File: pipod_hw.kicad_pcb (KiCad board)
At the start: 2 copper layers, 55.5 x 98.2 mm, 4 parts, among them J1 SFV8R-2STE1HLF, J2 SFV14R-2STE1HLF, J3 Conn_01x03_Male, J7 USB_C_Receptacle_USB2.0

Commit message: drc: set DRC for JLCPCB
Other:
- copper layers 2 -> 4
- board text added: "Layers: 4 PCB thickness: 0.8mm Impedance: Yes (JLC7628)"
- board text removed: "Board thickness: 0.8mm"
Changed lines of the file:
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@@
 (kicad_pcb (version 20211014) (generator pcbnew)
   (general
-    (thickness 1.6)
+    (thickness 0.7412)
   )
   (paper "A4")
   (layers
     (0 "F.Cu" signal)
+    (1 "In1.Cu" signal)
+    (2 "In2.Cu" signal)
     (31 "B.Cu" signal)
     (32 "B.Adhes" user "B.Adhesive")
@@
   )
   (setup
+    (stackup
+      (layer "F.SilkS" (type "Top Silk Screen") (color "White"))
+      (layer "F.Paste" (type "Top Solder Paste"))
+      (layer "F.Mask" (type "Top Solder Mask") (color "Purple") (thickness 0.01))
+      (layer "F.Cu" (type "copper") (thickness 0.035))
+      (layer "dielectric 1" (type "prepreg") (thickness 0.2104) (material "FR4") (epsilon_r 4.5) (loss_tangent 0.02))
+      (layer "In1.Cu" (type "copper") (thickness 0.0152))
+      (layer "dielectric 2" (type "core") (thickness 0.2) (material "FR4") (epsilon_r 4.5) (loss_tangent 0.02))
+      (layer "In2.Cu" (type "copper") (thickness 0.0152))
+      (layer "dielectric 3" (type "prepreg") (thickness 0.2104) (material "FR4") (epsilon_r 4.5) (loss_tangent 0.02))
+      (layer "B.Cu" (type "copper") (thickness 0.035))
+      (layer "B.Mask" (type "Bottom Solder Mask") (color "Purple") (thickness 0.01))
+      (layer "B.Paste" (type "Bottom Solder Paste"))
+      (layer "B.SilkS" (type "Bottom Silk Screen") (color "White"))
+      (copper_finish "None")
+      (dielectric_constraints yes)
+    )
     (pad_to_mask_clearance 0)
     (pcbplotparams
@@
     (effects (font (size 1 1) (thickness 0.15)) (justify left))
   )
-  (gr_text "Board thickness: 0.8mm" (at 133.9 29.2) (layer "Cmts.User")
-    (effects (font (size 5 5) (thickness 0.5)))
+  (gr_text "Layers: 4\nPCB thickness: 0.8mm\nImpedance: Yes (JLC7628)\n" (at 164.81 54.63) (layer "Cmts.User")
+    (effects (font (size 5 5) (thickness 0.5)) (justify left))
   )
   (segment (start 124.248 61.712) (end 124.256999 61.720999) (width 0.25) (layer "F.Cu") (net 0))

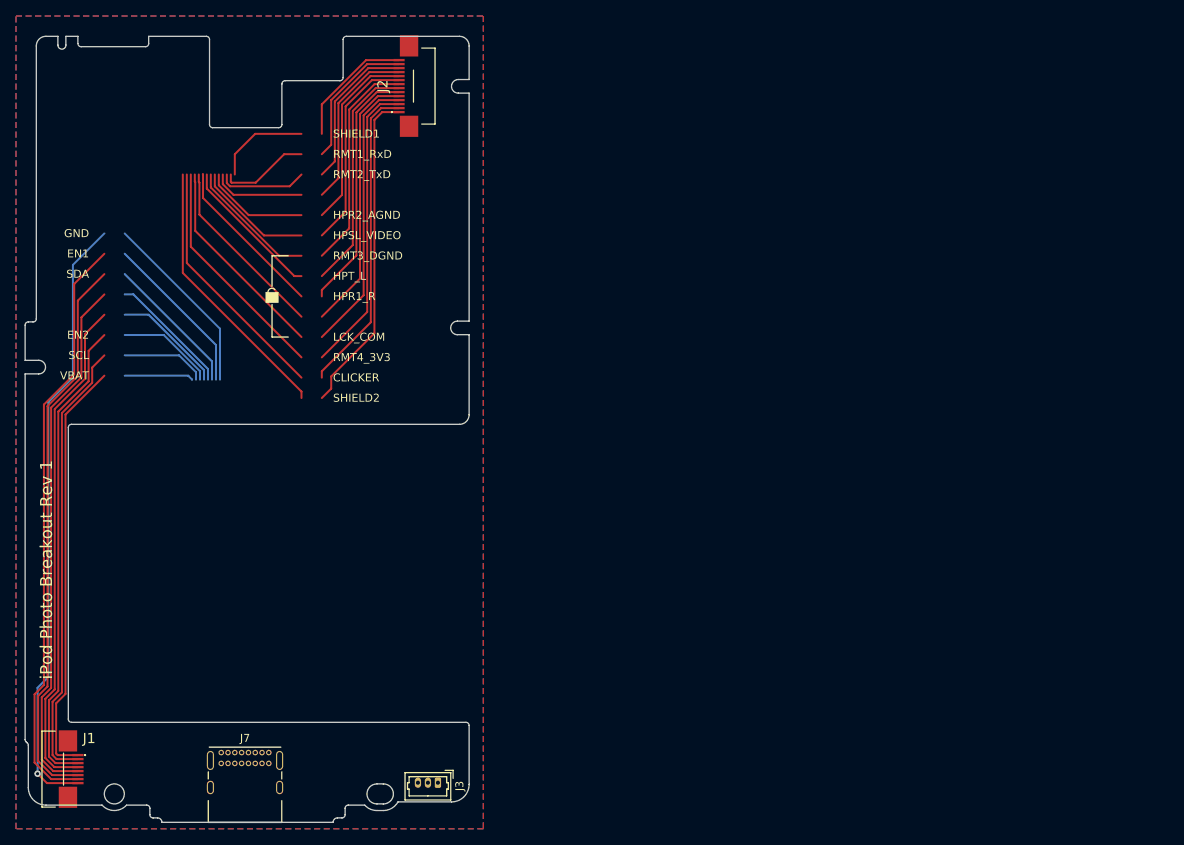
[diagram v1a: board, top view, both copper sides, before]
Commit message: analysis: specify pi will be powered directly from VCC
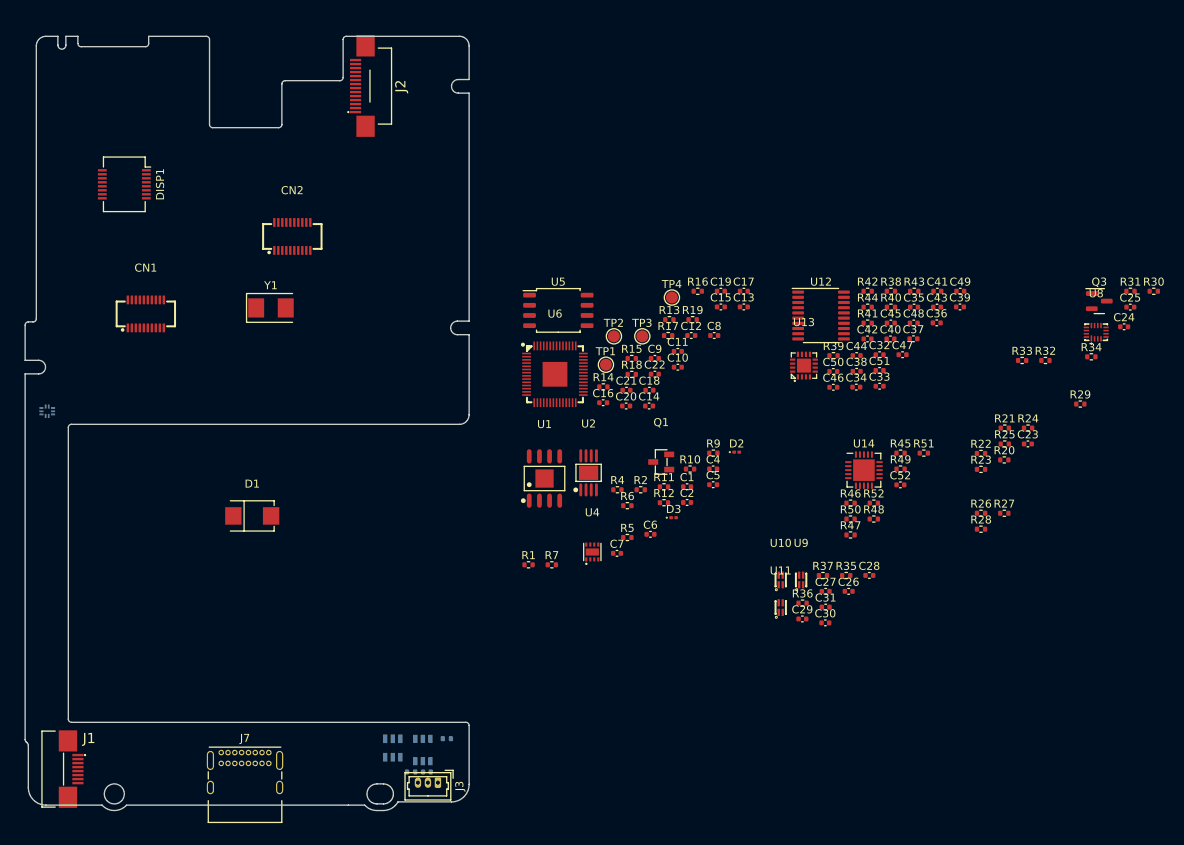
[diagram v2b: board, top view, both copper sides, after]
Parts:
- added C1: 100n, Capacitor_SMD:C_0402_1005Metric, F.Cu at (184.8, 100.7)
- added C10: 100n, Capacitor_SMD:C_0402_1005Metric, F.Cu at (183.6, 85.8)
- added C11: 100n, Capacitor_SMD:C_0402_1005Metric, F.Cu at (183.6, 83.8)
- added C12: 100n, Capacitor_SMD:C_0402_1005Metric, F.Cu at (185.3, 81.8)
- added C13: 100n, Capacitor_SMD:C_0402_1005Metric, F.Cu at (191.9, 78.3)
- added C14: 1u, Capacitor_SMD:C_0402_1005Metric, F.Cu at (180.0, 90.7)
- added C15: 100n, Capacitor_SMD:C_0402_1005Metric, F.Cu at (189.0, 78.3)
- added C16: 100n, Capacitor_SMD:C_0402_1005Metric, F.Cu at (174.3, 90.2)
- added C17: 100n, Capacitor_SMD:C_0402_1005Metric, F.Cu at (191.9, 76.3)
- added C18: 100n, Capacitor_SMD:C_0402_1005Metric, F.Cu at (180.1, 88.7)
- added C19: 100n, Capacitor_SMD:C_0402_1005Metric, F.Cu at (189.0, 76.3)
- added C2: 100n, Capacitor_SMD:C_0402_1005Metric, F.Cu at (184.8, 102.7)
- added C20: 1u, Capacitor_SMD:C_0402_1005Metric, F.Cu at (177.2, 90.7)
- added C21: 30p, Capacitor_SMD:C_0402_1005Metric, F.Cu at (177.2, 88.7)
- added C22: 30p, Capacitor_SMD:C_0402_1005Metric, F.Cu at (180.7, 86.7)
- added C23: 100n, Capacitor_SMD:C_0402_1005Metric, F.Cu at (227.4, 95.4)
- added C24: 100n, Capacitor_SMD:C_0402_1005Metric, F.Cu at (239.4, 80.8)
- added C25: 10u, Capacitor_SMD:C_0402_1005Metric, F.Cu at (240.2, 78.3)
- added C26: 10u, Capacitor_SMD:C_0402_1005Metric, F.Cu at (205.0, 113.8)
- added C27: 10u, Capacitor_SMD:C_0402_1005Metric, F.Cu at (202.1, 113.8)
- added C28: 10u, Capacitor_SMD:C_0402_1005Metric, F.Cu at (207.6, 111.8)
- added C29: 10u, Capacitor_SMD:C_0402_1005Metric, F.Cu at (199.2, 117.3)
- added C3: 100n, Capacitor_SMD:C_0402_1005Metric, B.Cu at (152.2, 136.4)
- added C30: 10u, Capacitor_SMD:C_0402_1005Metric, F.Cu at (202.1, 117.8)
- added C31: 10u, Capacitor_SMD:C_0402_1005Metric, F.Cu at (202.1, 115.8)
- added C32: 10u, Capacitor_SMD:C_0402_1005Metric, F.Cu at (208.8, 84.2)
- added C33: 100n, Capacitor_SMD:C_0402_1005Metric, F.Cu at (208.8, 88.2)
- added C34: 10u, Capacitor_SMD:C_0402_1005Metric, F.Cu at (205.9, 88.3)
- added C35: 100n, Capacitor_SMD:C_0402_1005Metric, F.Cu at (213.1, 78.3)
- added C36: 10u, Capacitor_SMD:C_0402_1005Metric, F.Cu at (216.0, 80.3)
- added C37: 100n, Capacitor_SMD:C_0402_1005Metric, F.Cu at (213.1, 82.2)
- added C38: 10u, Capacitor_SMD:C_0402_1005Metric, F.Cu at (206.0, 86.3)
- added C39: 2.2u, Capacitor_SMD:C_0402_1005Metric, F.Cu at (218.9, 78.3)
- added C4: 10u, Capacitor_SMD:C_0402_1005Metric, F.Cu at (188.0, 98.5)
- added C40: 2.2u, Capacitor_SMD:C_0402_1005Metric, F.Cu at (210.2, 82.3)
- added C41: 100n, Capacitor_SMD:C_0402_1005Metric, F.Cu at (216.1, 76.3)
- added C42: 10u, Capacitor_SMD:C_0402_1005Metric, F.Cu at (207.3, 82.3)
- added C43: 100n, Capacitor_SMD:C_0402_1005Metric, F.Cu at (216.0, 78.3)
- added C44: 1u, Capacitor_SMD:C_0402_1005Metric, F.Cu at (206.0, 84.3)
- added C45: 1u, Capacitor_SMD:C_0402_1005Metric, F.Cu at (210.2, 80.3)
- added C46: 2.2u, Capacitor_SMD:C_0402_1005Metric, F.Cu at (203.1, 88.3)
- added C47: 1u, Capacitor_SMD:C_0402_1005Metric, F.Cu at (211.7, 84.2)
- added C48: 1u, Capacitor_SMD:C_0402_1005Metric, F.Cu at (213.1, 80.3)
- added C49: 1u, Capacitor_SMD:C_0402_1005Metric, F.Cu at (218.9, 76.3)
- added C5: 100n, Capacitor_SMD:C_0402_1005Metric, F.Cu at (188.0, 100.5)
- added C50: 1u, Capacitor_SMD:C_0402_1005Metric, F.Cu at (203.1, 86.3)
- added C51: 1u, Capacitor_SMD:C_0402_1005Metric, F.Cu at (208.8, 86.2)
- added C52: 100n, Capacitor_SMD:C_0402_1005Metric, F.Cu at (211.4, 100.5)
- added C6: 100n, Capacitor_SMD:C_0402_1005Metric, F.Cu at (180.2, 106.7)
- added C7: 10u, Capacitor_SMD:C_0402_1005Metric, F.Cu at (176.0, 109.1)
- added C8: 100n, Capacitor_SMD:C_0402_1005Metric, F.Cu at (188.2, 81.8)
- added C9: 100n, Capacitor_SMD:C_0402_1005Metric, F.Cu at (180.7, 84.7)
- added CN1: 539160208, lcsc:CONN-SMD_539160208, F.Cu at (117.1, 79.1)
- added CN2: 539160208, lcsc:CONN-SMD_539160208, F.Cu at (135.4, 69.5)
- added D1: MBRS130LT3G, lcsc:SMB_L4.6-W3.6-LS5.3-RD, F.Cu at (130.4, 104.4)
- added D2: RED, LED_SMD:LED_0201_0603Metric, F.Cu at (191.0, 96.4)
- added D3: GRN, LED_SMD:LED_0201_0603Metric, F.Cu at (183.1, 104.6)
- added DISP1: STP240320_0200B, Connector_Molex:Molex_SlimStack_54722-0164_2x08_P0.50mm_Vertical, F.Cu at (114.4, 62.9)
- added Q1: DMP1045U-7, lcsc:SOT-23-3_L2.9-W1.3-P1.90-LS2.4-BR, F.Cu at (181.5, 97.7)
- added Q2: UMW8205A, lcsc:SOT-23-6_L2.9-W1.6-P0.95-LS2.8-BL, B.Cu at (148.0, 133.4)
- added Q3: BSS138, Package_TO_SOT_SMD:SOT-23, F.Cu at (236.3, 77.5)
- added R1: 10k, Resistor_SMD:R_0402_1005Metric, F.Cu at (164.9, 110.5)
- added R10: 10k, Resistor_SMD:R_0402_1005Metric, F.Cu at (185.1, 98.5)
- added R11: 5.36k, Resistor_SMD:R_0402_1005Metric, F.Cu at (181.9, 100.8)
- added R12: 1.62k, Resistor_SMD:R_0402_1005Metric, F.Cu at (181.9, 102.7)
- added R13: 10k, Resistor_SMD:R_0402_1005Metric, F.Cu at (182.6, 79.9)
- added R14: DNP, Resistor_SMD:R_0402_1005Metric, F.Cu at (174.3, 88.3)
- added R15: 1k, Resistor_SMD:R_0402_1005Metric, F.Cu at (177.8, 84.7)
- added R16: 10k, Resistor_SMD:R_0402_1005Metric, F.Cu at (186.1, 76.3)
- added R17: 27R, Resistor_SMD:R_0402_1005Metric, F.Cu at (182.4, 81.8)
- added R18: 27R, Resistor_SMD:R_0402_1005Metric, F.Cu at (177.8, 86.7)
- added R19: 10k, Resistor_SMD:R_0402_1005Metric, F.Cu at (185.5, 79.9)
- added R2: 1.62k 2%, Resistor_SMD:R_0402_1005Metric, F.Cu at (179.0, 101.1)
- added R20: DNP, Resistor_SMD:R_0402_1005Metric, F.Cu at (224.4, 97.4)
- added R21: 10k, Resistor_SMD:R_0402_1005Metric, F.Cu at (224.5, 93.4)
- added R22: 15k, Resistor_SMD:R_0402_1005Metric, F.Cu at (221.5, 96.6)
- added R23: 5.1k, Resistor_SMD:R_0402_1005Metric, F.Cu at (221.5, 98.6)
- added R24: 5.1k, Resistor_SMD:R_0402_1005Metric, F.Cu at (227.4, 93.4)
- added R25: 10k, Resistor_SMD:R_0402_1005Metric, F.Cu at (224.5, 95.4)
- added R26: 10k, Resistor_SMD:R_0402_1005Metric, F.Cu at (221.5, 104.1)
- added R27: 100k, Resistor_SMD:R_0402_1005Metric, F.Cu at (224.4, 104.1)
- added R28: 10k, Resistor_SMD:R_0402_1005Metric, F.Cu at (221.5, 106.0)
- added R29: 10k, Resistor_SMD:R_0402_1005Metric, F.Cu at (233.9, 90.4)
- added R3: 1k, Resistor_SMD:R_0402_1005Metric, B.Cu at (154.7, 132.2)
- added R30: 0R, Resistor_SMD:R_0402_1005Metric, F.Cu at (243.1, 76.3)
- added R31: 10k, Resistor_SMD:R_0402_1005Metric, F.Cu at (240.2, 76.3)
- added R32: 10k, Resistor_SMD:R_0402_1005Metric, F.Cu at (229.6, 85.0)
- added R33: 10R, Resistor_SMD:R_0402_1005Metric, F.Cu at (226.7, 85.0)
- added R34: 0R, Resistor_SMD:R_0402_1005Metric, F.Cu at (235.3, 84.5)
- added R35: 10k, Resistor_SMD:R_0402_1005Metric, F.Cu at (204.7, 111.8)
- added R36: 10k, Resistor_SMD:R_0402_1005Metric, F.Cu at (199.2, 115.3)
- added R37: 10k, Resistor_SMD:R_0402_1005Metric, F.Cu at (201.8, 111.8)
- added R38: 10k, Resistor_SMD:R_0402_1005Metric, F.Cu at (210.2, 76.3)
- added R39: 10k, Resistor_SMD:R_0402_1005Metric, F.Cu at (203.1, 84.4)
- added R4: 5.62k 2%, Resistor_SMD:R_0402_1005Metric, F.Cu at (176.1, 101.1)
- added R40: 10k, Resistor_SMD:R_0402_1005Metric, F.Cu at (210.2, 78.3)
- added R41: 10k, Resistor_SMD:R_0402_1005Metric, F.Cu at (207.3, 80.3)
- added R42: 10k, Resistor_SMD:R_0402_1005Metric, F.Cu at (207.3, 76.3)
- added R43: 10k, Resistor_SMD:R_0402_1005Metric, F.Cu at (213.2, 76.3)
- added R44: 10k, Resistor_SMD:R_0402_1005Metric, F.Cu at (207.3, 78.3)
- added R45: 10k, Resistor_SMD:R_0402_1005Metric, F.Cu at (211.4, 96.5)
- added R46: 0R, Resistor_SMD:R_0402_1005Metric, F.Cu at (205.2, 102.8)
- added R47: 0R, Resistor_SMD:R_0402_1005Metric, F.Cu at (205.2, 106.8)
- added R48: 0R, Resistor_SMD:R_0402_1005Metric, F.Cu at (208.1, 104.8)
- added R49: 0R, Resistor_SMD:R_0402_1005Metric, F.Cu at (211.4, 98.5)
- added R5: 1.27M 2%, Resistor_SMD:R_0402_1005Metric, F.Cu at (177.3, 107.1)
- added R50: 0R, Resistor_SMD:R_0402_1005Metric, F.Cu at (205.2, 104.8)
- added R51: 0R, Resistor_SMD:R_0402_1005Metric, F.Cu at (214.4, 96.5)
- added R52: 0R, Resistor_SMD:R_0402_1005Metric, F.Cu at (208.1, 102.8)
- added R6: 1k, Resistor_SMD:R_0402_1005Metric, F.Cu at (177.3, 103.1)
- added R7: 1k, Resistor_SMD:R_0402_1005Metric, F.Cu at (167.9, 110.5)
- added R8: 470R, Resistor_SMD:R_0402_1005Metric, B.Cu at (150.3, 136.4)
- added R9: 10k, Resistor_SMD:R_0402_1005Metric, F.Cu at (188.1, 96.5)
- added TP1: TestPoint, TestPoint:TestPoint_Pad_D1.5mm, F.Cu at (174.6, 85.5)
- added TP2: TestPoint, TestPoint:TestPoint_Pad_D1.5mm, F.Cu at (175.6, 81.9)
- added TP3: TestPoint, TestPoint:TestPoint_Pad_D1.5mm, F.Cu at (179.2, 81.9)
- added TP4: TestPoint, TestPoint:TestPoint_Pad_D1.5mm, F.Cu at (182.9, 77.1)
- added U1: TD5830B, lcsc:SOP-8_L4.9-W3.9-P1.27-LS6.0-BL-EP, F.Cu at (166.9, 99.7)
- added U10: SY6283ADRC, lcsc:DFN-4_L1.6-W1.2-P0.50-BL, F.Cu at (196.5, 112.4)
- added U11: SY6283ADRC, lcsc:DFN-4_L1.6-W1.2-P0.50-BL, F.Cu at (196.5, 115.8)
- added U12: PCM5102, Package_SO:TSSOP-20_4.4x6.5mm_P0.65mm, F.Cu at (201.5, 79.3)
- added U13: PAM8908JER, lcsc:QFN-16_L3.0-W3.0-P0.50-BL-EP1.7, F.Cu at (199.4, 85.6)
- added U14: MCP23008-xML, Package_DFN_QFN:QFN-20-1EP_4x4mm_P0.5mm_EP2.7x2.7mm, F.Cu at (206.9, 98.7)
- added U2: TP4056M, lcsc:MSOP-8_L3.0-W3.0-P0.65-LS5.0-BL-EP, F.Cu at (172.5, 99.0)
- added U3: DW01A-G, lcsc:SOT-23-6_L2.9-W1.6-P0.95-LS2.8-BR, B.Cu at (151.7, 133.7)
- added U4: MAX17048G+T10, lcsc:DFN-8_L2.0-W2.0-P0.50-BL-EP, F.Cu at (172.9, 108.9)
- added U5: W25Q128JVS, Package_SO:SOIC-8_5.23x5.23mm_P1.27mm, F.Cu at (168.7, 78.7)
- added U6: RP2040, lcsc:LQFN-56_L7.0-W7.0-P0.4-EP, F.Cu at (168.2, 86.7)
- added U7: PI3USB102EZLEX, lcsc:TQFN-10_L1.6-W1.3-P0.50-BL, B.Cu at (104.8, 91.3)
- added U8: TS3A5018RSVR, lcsc:UQFN-16_L2.6-W1.8-P0.40-BL, F.Cu at (235.9, 81.4)
- added U9: SY6283ADRC, lcsc:DFN-4_L1.6-W1.2-P0.50-BL, F.Cu at (199.0, 112.4)
- added Y1: 12MHz 20pF, Crystal:Crystal_SMD_5032-2Pin_5.0x3.2mm, F.Cu at (132.8, 78.4)
- moved J2 5.44 mm to (145.1, 50.7)
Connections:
- net Net-(J7-PadA4) renamed VBUS
- J1 pad 1: unconnected-(J1-Pad1) -> +3V3
- J1 pad 2: unconnected-(J1-Pad2) -> SMC_CW_SCK
- J1 pad 3: unconnected-(J1-Pad3) -> CW_EN1
- J1 pad 6: unconnected-(J1-Pad6) -> SMC_CW_MOSI
- J1 pad 7: unconnected-(J1-Pad7) -> CW_EN2
- J1 pad 8: unconnected-(J1-Pad8) -> GND
- J2 pad 1: unconnected-(J2-Pad1) -> HP_SHIELD
- J2 pad 10: unconnected-(J2-Pad10) -> GNDA
- J2 pad 12: unconnected-(J2-Pad12) -> SMC_RMT_TX
- J2 pad 13: unconnected-(J2-Pad13) -> SMC_RMT_RX
- J2 pad 14: unconnected-(J2-Pad14) -> HP_SHIELD
- J2 pad 2: unconnected-(J2-Pad2) -> HP_CLICKER
- J2 pad 3: unconnected-(J2-Pad3) -> HP_RMT4_3V3
- J2 pad 4: unconnected-(J2-Pad4) -> HP_LCK
- J2 pad 6: unconnected-(J2-Pad6) -> HP_R1_R
- J2 pad 7: unconnected-(J2-Pad7) -> HP_T_L
- J2 pad 8: unconnected-(J2-Pad8) -> GND
- J2 pad 9: unconnected-(J2-Pad9) -> HP_SL_VIDEO
- J7 pad A1: Net-(J7-PadA1) -> GND
- J7 pad A12: Net-(J7-PadA1) -> GND
- J7 pad A5: unconnected-(J7-PadA5) -> USB_CC1
- J7 pad A6: unconnected-(J7-PadA6) -> USB_D+
- J7 pad A7: unconnected-(J7-PadA7) -> USB_D-
- J7 pad B1: Net-(J7-PadA1) -> GND
- J7 pad B12: Net-(J7-PadA1) -> GND
- J7 pad B5: unconnected-(J7-PadB5) -> USB_CC2
- J7 pad B6: unconnected-(J7-PadB6) -> USB_D+
- J7 pad B7: unconnected-(J7-PadB7) -> USB_D-
- J7 pad S1: unconnected-(J7-PadS1) -> Net-(J7-PadS1)
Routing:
- net (no net): track 394.7 -> 0.00 mm
- net unconnected-(J1-Pad8): track 76.5 -> 0.00 mm, vias 1 -> 0
- net unconnected-(J1-Pad7): track 73.5 -> 0.00 mm
- net unconnected-(J1-Pad6): track 70.0 -> 0.00 mm
- net unconnected-(J1-Pad5): track 66.5 -> 0.00 mm
- net unconnected-(J1-Pad4): track 63.0 -> 0.00 mm
- net unconnected-(J1-Pad3): track 59.5 -> 0.00 mm
- net unconnected-(J1-Pad2): track 56.0 -> 0.00 mm
- net unconnected-(J1-Pad1): track 52.5 -> 0.00 mm
- net unconnected-(J2-Pad1): track 41.0 -> 0.00 mm
- net unconnected-(J2-Pad2): track 39.0 -> 0.00 mm
- net unconnected-(J2-Pad3): track 37.1 -> 0.00 mm
- net unconnected-(J2-Pad4): track 35.1 -> 0.00 mm
- net unconnected-(J2-Pad5): track 33.1 -> 0.00 mm
- net unconnected-(J2-Pad6): track 31.2 -> 0.00 mm
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- added copper zone on In2.Cu, net +3V3
- added copper zone on In1.Cu, net GND
- removed copper zone on B.Cu, net (none)
- removed copper zone on F.Cu, net (none)
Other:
- board size 55.5 x 98.2 mm -> 55.5 x 96.8 mm
- board text removed: "CLICKER"
- board text removed: "EN1"
- board text removed: "EN2"
- board text removed: "GND"
- board text removed: "HPR1_R"
- board text removed: "HPR2_AGND"
- board text removed: "HPSL_VIDEO"
- board text removed: "HPT_L"
- board text removed: "LCK_COM"
- board text removed: "NOTE: CLICKWHEEL IS NOT AN I2C DEVICE. See https://jasongarr.wordpress.com/project-pages/ipod-clickwheel-hack/ for more info"
- board text removed: "RMT1_RxD"
- board text removed: "RMT2_TxD"
- board text removed: "RMT3_DGND"
- board text removed: "RMT4_3V3"
- board text removed: "SCL"
- board text removed: "SDA"
- board text removed: "SHIELD1"
- board text removed: "SHIELD2"
- board text removed: "VBAT"
- board text removed: "iPod Photo Breakout Rev 1"

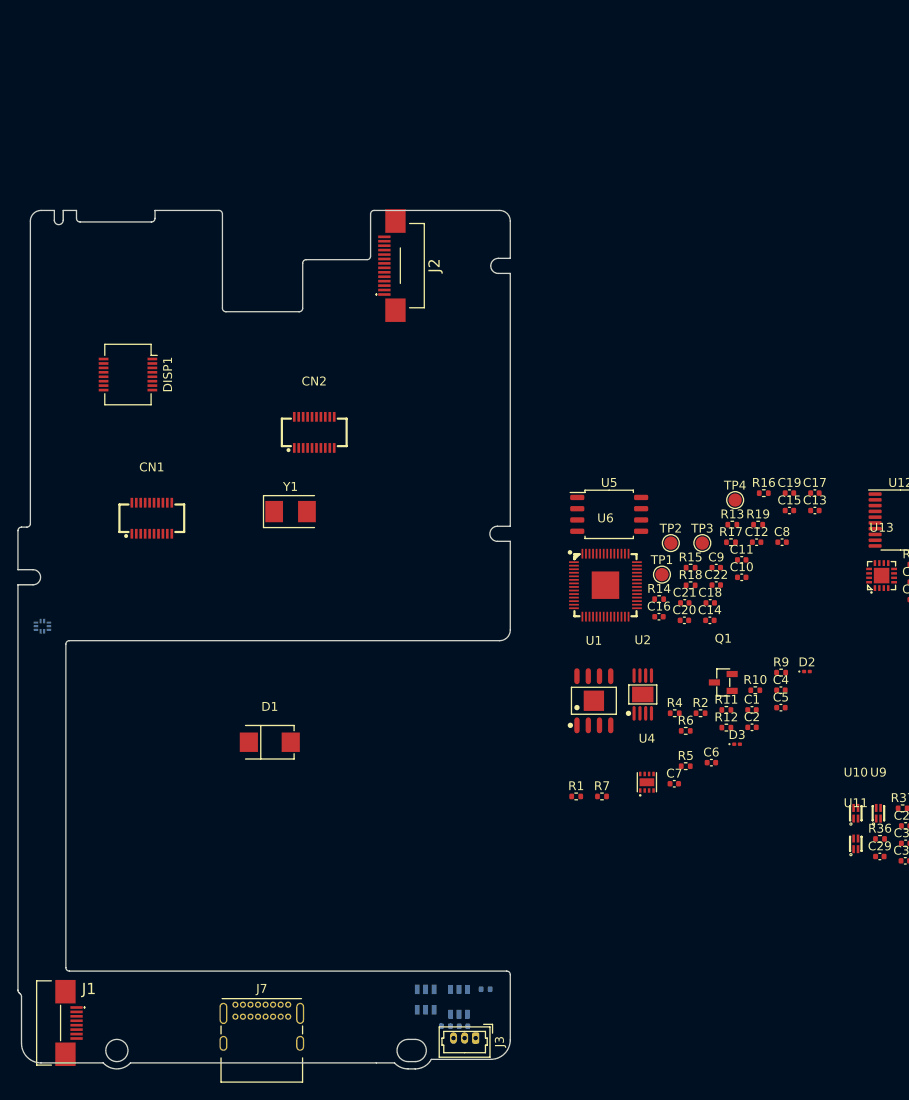
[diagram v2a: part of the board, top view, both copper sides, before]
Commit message: layout: switch to lcsc fpc connectors
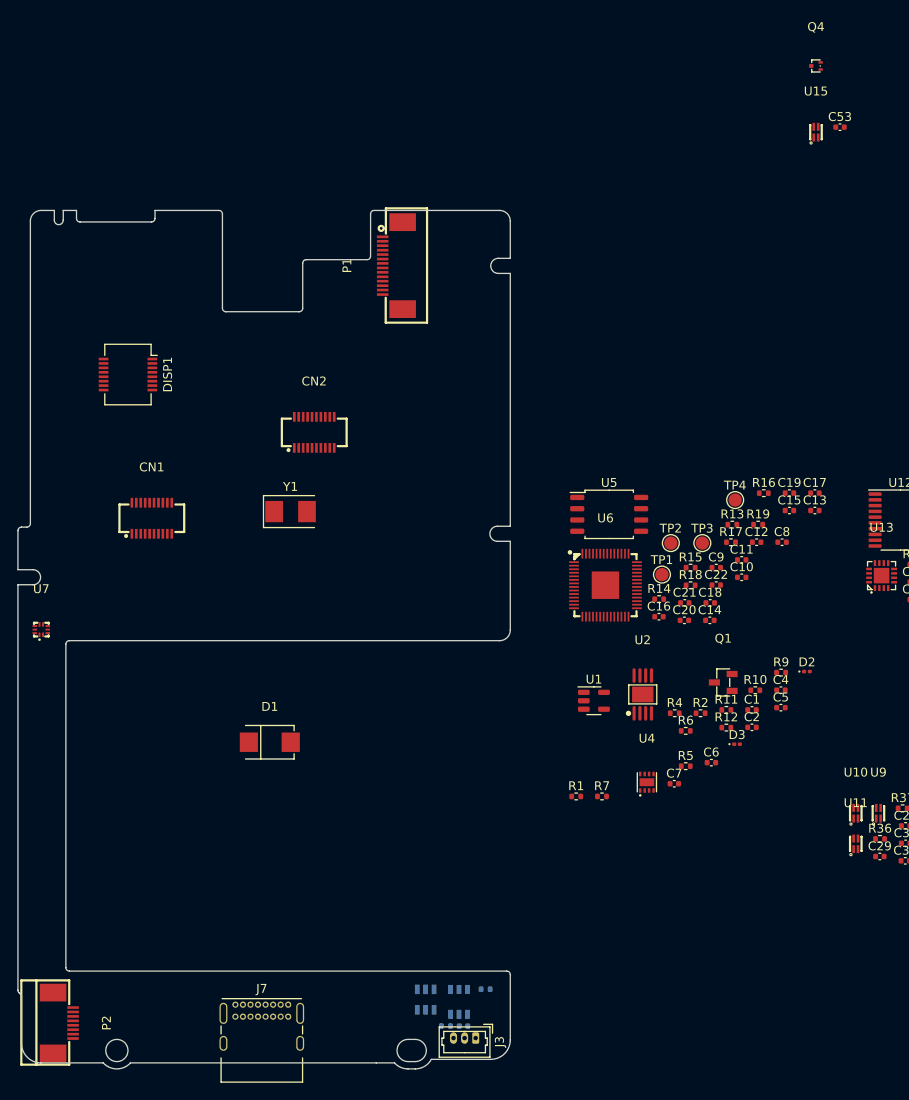
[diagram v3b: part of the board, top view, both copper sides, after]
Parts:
- removed J1: SFV8R-2STE1HLF, Gigahawk:SFV8R2STE1HLF
- removed J2: SFV14R-2STE1HLF, Gigahawk:SFV14R2STE1HLF
- added C53: 10u, Capacitor_SMD:C_0402_1005Metric, F.Cu at (194.7, 35.1)
- added P1: FPC0.5MM14PPulltypeH2.0mmPickup, lcsc:FPC-SMD_14P-L12.5-W5.4-P0.50, F.Cu at (144.3, 50.7)
- added P2: FPC0.5MM8PPulltypeH2.0mmPickup, lcsc:FPC-SMD_AFC07-S08ECC-00, F.Cu at (107.0, 136.0)
- added Q4: TPNTK3139PT1G, lcsc:SOT-723_L1.2-W0.8-P0.40-LS1.2-BR, F.Cu at (192.0, 28.2)
- added U15: SY6283ADRC, lcsc:DFN-4_L1.6-W1.2-P0.50-BL, F.Cu at (192.0, 35.6)
- C6: value 100n -> 10u
- R11: value 5.36k -> DNI
- U1: value TD5830B -> XC6210B332MR; footprint lcsc:SOP-8_L4.9-W3.9-P1.27-LS6.0-BL-EP -> Package_TO_SOT_SMD:SOT-23-5
- U7: moved to F.Cu
- moved U7 0.41 mm to (104.6, 91.7), turned to 0 degrees
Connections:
- C26 pad 2: +3V3 -> VCC
- C32 pad 1: PI_VCC -> AUDIO_3V3
- C33 pad 1: PI_VCC -> AUDIO_3V3
- C34 pad 1: PI_VCC -> AUDIO_3V3
- C35 pad 1: PI_VCC -> AUDIO_3V3
- C36 pad 1: PI_VCC -> AUDIO_3V3
- C37 pad 1: PI_VCC -> AUDIO_3V3
- C38 pad 1: PI_VCC -> AUDIO_3V3
- C41 pad 1: PI_VCC -> AUDIO_3V3
- C46 pad 2: PI_VCC -> AUDIO_3V3
- C52 pad 2: PI_VCC -> AUDIO_3V3
- C6 pad 2: Net-(C6-Pad2) -> GND
- C7 pad 1: +3V3 -> GND
- C7 pad 2: GND -> +3V3
- R11 pad 1: +3V3 -> GND
- R11 pad 2: Net-(C6-Pad2) -> Net-(R11-Pad2)
- R45 pad 1: PI_VCC -> AUDIO_3V3
- R9 pad 1: +3V3 -> Net-(R11-Pad2)
- R9 pad 2: PGOOD -> VCC
- U1 pad 1: PGOOD -> VCC
- U1 pad 2: VCC -> GND
- U1 pad 3: VCC -> Net-(R11-Pad2)
- U1 pad 4: VCC -> unconnected-(U1-Pad4)
- U1 pad 5: unconnected-(U1-Pad5) -> +3V3
- U12 pad 1: PI_VCC -> AUDIO_3V3
- U12 pad 20: PI_VCC -> AUDIO_3V3
- U12 pad 8: PI_VCC -> AUDIO_3V3
- U13 pad 14: PI_VCC -> AUDIO_3V3
- U14 pad 18: PI_VCC -> AUDIO_3V3
- U6 pad 37: PGOOD -> unconnected-(U6-Pad37)
- U9 pad 3: +3V3 -> VCC

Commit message: integration: add mounting holes and connectors and second board
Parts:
- removed CN1, CN2: 539160208, lcsc:CONN-SMD_539160208
- added FPC1: 527462033, lcsc:FPC-SMD_527462033, F.Cu at (49.0, 30.0)
- added FPC2: 527462033, lcsc:FPC-SMD_527462033, F.Cu at (37.0, 41.0)
- added H1: MountingHole_PiPod, pipod_hw:MountingHole_PiPod, F.Cu at (0.00, 0.00)
- added R53: 10k, Resistor_SMD:R_0402_1005Metric, F.Cu at (251.1, 50.0)
- R12: value 1.62k -> DNI
- moved C1 112.6 mm to (81.3, 56.3)
- moved C10 112.6 mm to (80.2, 41.4)
- moved C11 112.6 mm to (80.2, 39.4)
- moved C13 112.6 mm to (88.4, 33.8)
- moved C14 112.6 mm to (76.6, 46.2)
- moved C15 112.6 mm to (85.6, 33.8)
- moved C17 112.6 mm to (88.4, 31.9)
- moved C19 112.6 mm to (85.6, 31.9)
- moved C22 112.6 mm to (77.3, 42.2)
- moved C24 112.6 mm to (136.0, 36.3)
- moved C28 112.6 mm to (104.1, 67.4)
- moved C3 112.6 mm to (48.8, 92.0)
- moved C30 112.6 mm to (98.6, 73.3)
- moved C32 112.6 mm to (105.4, 39.8)
- moved C33 112.6 mm to (105.4, 43.7)
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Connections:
- R12 pad 1: Net-(C6-Pad2) -> HP_CLICKER
- R12 pad 2: GND -> Net-(P1-Pad13)
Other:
- outline, holes or cut-outs redrawn
